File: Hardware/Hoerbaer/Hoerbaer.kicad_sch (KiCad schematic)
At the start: 41 parts, among them J1 I2C, J11 UART, J13 JTAG, J17 RST_BOOT, J2 DISPLAY, J3 uSD, J4 USB1, J5 ENCODER, SW1 RESET, SW2 PROG, U1 ESP32 S3 MINI

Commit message: Sleeping...
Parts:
- renumbered C50 to C1, C50 to C2, C50 to C3, C50 to C4, C43 to C64

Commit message: WIP new hw rev
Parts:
- removed D4: GREEN, LED_SMD:LED_0603_1608Metric, symbol Device:LED
- removed J13: JTAG, Connector_PinHeader_1.27mm:PinHeader_2x05_P1.27mm_Vertical_SMD, symbol Connector_Generic:Conn_02x05_Odd_Even
- removed R56: 5.1kΩ, Resistor_SMD:R_0402_1005Metric, symbol Device:R_Small
- removed U1: ESP32 S3 MINI, ESP32-S3-MINI-1-N8:XCVR_ESP32-S3-MINI-1-N8, symbol Baer_Symbols:ESP32-S3-MINI-1-N8
- added H4: MountingHole_Pad, MountingHole:MountingHole_3.2mm_M3_Pad_Via, symbol Mechanical:MountingHole_Pad
- added U1: ESP32-S3-WROOM-1U-N4R8, RF_Module:ESP32-S3-WROOM-1, symbol Baer_Symbols:ESP32-S3-WROOM-1
- C1, C4, C5: value 1µF, 10V -> 1µF, 16V; LCSC C29266 -> C29266
- renumbered C64 to C6, D8 to D1, D1 to D2, D2 to D3, J3 to J2, J4 to J3, J2 to J4, J11 to J5, J17 to J6, J5 to J7, R12 to R10, R14 to R11, R15 to R12, R16 to R13, R13 to R14, R10 to R15, R8 to R16, R9 to R8, R11 to R9
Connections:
- net 3V3_~{PSAVE}: now also U1.26 (IO45)
- net BAT_~{ALERT}: now also U1.16 (IO46)
- net CHG_STAT: now also U1.24 (IO47)
- net CODEC_~{PDN}: now also U1.39 (IO1)
- net DISP_CS: now also U1.5 (IO5)
- net DISP_DC: now also U1.6 (IO6)
- net DISP_RST: now also U1.7 (IO7)
- net ENC_A: now also U1.9 (IO16)
- net ENC_B: now also U1.10 (IO17)
- net ENC_BTN: now also U1.11 (IO18)
- net GND: now also H4.1, U1.1 (GND), U1.40 (GND), U1.41 (GND)
- net HBI_INT: now also U1.8 (IO15)
- net HBI_RST: now also U1.22 (IO14)
- net I2C1_SCL: now also U1.19 (IO11)
- net I2C1_SDA: now also U1.18 (IO10)
- net I2S1_BCLK: now also U1.38 (IO2)
- net I2S1_DOUT: now also U1.4 (IO4)
- net I2S1_WS: now also U1.15 (IO3)
- net MCU_IO0: now also U1.27 (IO0)
- net MCU_RXD: now also U1.36 (RXD0)
- net MCU_TXD: now also U1.37 (TXD0)
- net MCU_~{RST}: now also U1.3 (EN)
- net SD_CLK: now also U1.21 (IO13)
- net SD_CMD: now also U1.20 (IO12)
- net SD_D0: now also U1.31 (IO38)
- net SD_D1: now also U1.32 (IO39)
- net SD_D2: now also U1.33 (IO40)
- net SD_D3: now also U1.34 (IO41)
- net SD_DET: now also U1.23 (IO21)
- net SPI2_CLK: now also U1.17 (IO9)
- net SPI2_MOSI: now also U1.12 (IO8)
- net USB1_D+: now also U1.14 (USB_D+)
- net USB1_D-: now also U1.13 (USB_D-)
- net VCC: now also U1.2 (3V3); no longer C1.1, J1.4 (Pin_4), J2.4 (VDD), J4.7 (Pin_7), R1.1, R10.1, R11.1, R15.1, R16.1, R2.1, R3.1, R4.1, R7.1, R8.1, R9.1
- new net 9V_EN: U1.35 (IO42)
- new net VCC_P: C1.1, J1.4 (Pin_4), J2.4 (VDD), J4.7 (Pin_7), R1.1, R10.1, R11.1, R15.1, R16.1, R2.1, R3.1, R4.1, R7.1, R8.1, R9.1
- new net VCC_P_EN: U1.25 (IO48)
- no-connect marks 4 -> 6
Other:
- sheet Power ports: added 9V_EN, CHG_PGOOD, VCC_P_EN; removed 12V_EN
- moved on the sheet: C5, C6, J7, R14, R15, R16

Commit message: Layout, mono-jumpers
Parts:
- removed H4: MountingHole_Pad, MountingHole:MountingHole_3.2mm_M3_Pad_Via, symbol Mechanical:MountingHole_Pad
- J2: footprint Connector_Card:microSD_HC_Molex_104031-0811 -> Connector_Card:microSD_HC_Hirose_DM3D-SF; LCSC C585350 -> C719027; MPN 1040310811 -> DM3D-SF
- U1: value ESP32-S3-WROOM-1U-N4R8 -> ESP32-S3-WROOM-1-N4R8; LCSC C3013943 -> C2913200; MPN ESP32-S3-WROOM-1U-N4R8 -> ESP32-S3-WROOM-1-N4R8
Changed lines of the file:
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@@
 			)
 		)
-		(property "Footprint" "Connector_Card:microSD_HC_Molex_104031-0811"
+		(property "Footprint" "Connector_Card:microSD_HC_Hirose_DM3D-SF"
 			(at -5.08 152.4 0)
 			(effects
@@
 			)
 		)
-		(property "MPN" "1040310811"
+		(property "MPN" "DM3D-SF"
 			(at 46.99 170.18 0)
 			(effects
@@
 			)
 		)
-		(property "LCSC" "C585350"
+		(property "LCSC" "C719027"
 			(at 46.99 170.18 0)
 			(effects
@@
 	(symbol
 		(lib_id "Mechanical:MountingHole_Pad")
-		(at 209.55 158.75 0)
-		(unit 1)
-		(exclude_from_sim no)
-		(in_bom no)
-		(on_board yes)
-		(dnp no)
-		(fields_autoplaced yes)
-		(property "Reference" "H4"
-			(at 212.09 156.21 0)
-			(effects
-				(font
-					(size 1.27 1.27)
-				)
-				(justify left)
-				(hide yes)
-			)
-		)
-		(property "Value" "MountingHole_Pad"
-			(at 212.09 158.75 0)
-			(effects
-				(font
-					(size 1.27 1.27)
-				)
-				(justify left)
-				(hide yes)
-			)
-		)
-		(property "Footprint" "MountingHole:MountingHole_3.2mm_M3_Pad_Via"
-			(at 209.55 158.75 0)
-			(effects
-				(font
-					(size 1.27 1.27)
-				)
-				(hide yes)
-			)
-		)
-		(property "Datasheet" "~"
-			(at 209.55 158.75 0)
-			(effects
-				(font
-					(size 1.27 1.27)
-				)
-				(hide yes)
-			)
-		)
-		(property "Description" ""
-			(at 209.55 158.75 0)
-			(effects
-				(font
-					(size 1.27 1.27)
-				)
-			)
-		)
-		(property "Check_prices" ""
-			(at 209.55 158.75 0)
-			(effects
-				(font
-					(size 1.27 1.27)
-				)
-			)
-		)
-		(property "MANUFACTURER" ""
-			(at 209.55 158.75 0)
-			(effects
-				(font
-					(size 1.27 1.27)
-				)
-			)
-		)
-		(property "MAXIMUM_PACKAGE_HEIGHT" ""
-			(at 209.55 158.75 0)
-			(effects
-				(font
-					(size 1.27 1.27)
-				)
-			)
-		)
-		(property "MF" ""
-			(at 209.55 158.75 0)
-			(effects
-				(font
-					(size 1.27 1.27)
-				)
-			)
-		)
-		(property "MP" ""
-			(at 209.55 158.75 0)
-			(effects
-				(font
-					(size 1.27 1.27)
-				)
-			)
-		)
-		(property "PARTREV" ""
-			(at 209.55 158.75 0)
-			(effects
-				(font
-					(size 1.27 1.27)
-				)
-			)
-		)
-		(property "Package" ""
-			(at 209.55 158.75 0)
-			(effects
-				(font
-					(size 1.27 1.27)
-				)
-			)
-		)
-		(property "Price" ""
-			(at 209.55 158.75 0)
-			(effects
-				(font
-					(size 1.27 1.27)
-				)
-			)
-		)
-		(property "Purchase-URL" ""
-			(at 209.55 158.75 0)
-			(effects
-				(font
-					(size 1.27 1.27)
-				)
-			)
-		)
-		(property "STANDARD" ""
-			(at 209.55 158.75 0)
-			(effects
-				(font
-					(size 1.27 1.27)
-				)
-			)
-		)
-		(property "SnapEDA_Link" ""
-			(at 209.55 158.75 0)
-			(effects
-				(font
-					(size 1.27 1.27)
-				)
-			)
-		)
-		(pin "1"
-		)
-		(instances
-			(project "Hoerbaer"
-				(path "/31f16f54-0469-45ae-b442-d363bf5fad3b"
-					(reference "H4")
-					(unit 1)
-				)
-			)
-		)
-	)
-	(symbol
-		(lib_id "Mechanical:MountingHole_Pad")
 		(at 194.31 158.75 0)
 		(unit 1)
@@
 			)
 		)
-		(property "Value" "ESP32-S3-WROOM-1U-N4R8"
+		(property "Value" "ESP32-S3-WROOM-1-N4R8"
 			(at 142.748 73.66 0)
 			(effects
@@
 			)
 		)
-		(property "LCSC" "C3013943"
+		(property "LCSC" "C2913200"
 			(at 154.94 106.68 0)
 			(effects
@@
 			)
 		)
-		(property "MPN" "ESP32-S3-WROOM-1U-N4R8 "
+		(property "MPN" "ESP32-S3-WROOM-1-N4R8"
 			(at 154.94 106.68 0)
 			(effects
@@
 					(unit 1)
 				)
-			)
-		)
-	)
-	(symbol
-		(lib_id "power:GND")
-		(at 209.55 161.29 0)
-		(mirror y)
-		(unit 1)
-		(exclude_from_sim no)
-		(in_bom yes)
-		(on_board yes)
-		(dnp no)
-		(property "Reference" "#PWR0199"
-			(at 209.55 167.64 0)
-			(effects
-				(font
-					(size 1.27 1.27)
-				)
-				(hide yes)
-			)
-		)
-		(property "Value" "GND"
-			(at 213.36 163.83 0)
-			(effects
-				(font
-					(size 1.27 1.27)
-				)
-			)
-		)
-		(property "Footprint" ""
-			(at 209.55 161.29 0)
-			(effects
-				(font
-					(size 1.27 1.27)
-				)
-				(hide yes)
-			)
-		)
-		(property "Datasheet" ""
-			(at 209.55 161.29 0)
-			(effects
-				(font
-					(size 1.27 1.27)
-				)
-				(hide yes)
-			)
-		)
-		(property "Description" ""
-			(at 209.55 161.29 0)
-			(effects
-				(font
-					(size 1.27 1.27)
-				)
-			)
-		)
-		(pin "1"
-		)
-		(instances
-			(project "Hoerbaer"
-				(path "/31f16f54-0469-45ae-b442-d363bf5fad3b"
-					(reference "#PWR0199")
-					(unit 1)
-				)

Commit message: Layout rev 2 - without silkscreen
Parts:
- J1: footprint Connector_PinHeader_2.54mm:PinHeader_1x04_P2.54mm_Vertical -> Connector_PinHeader_2.54mm:PinHeader_2x02_P2.54mm_Vertical
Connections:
- net BAT_~{ALERT}: now also U1.39 (IO1); no longer U1.16 (IO46)
- net CODEC_~{PDN}: now also U1.22 (IO14); no longer U1.39 (IO1)
- net DISP_CS: now also U1.11 (IO18); no longer U1.5 (IO5)
- net DISP_DC: now also U1.12 (IO8); no longer U1.6 (IO6)
- net DISP_RST: now also U1.38 (IO2); no longer U1.7 (IO7)
- net ENC_A: now also U1.4 (IO4); no longer U1.9 (IO16)
- net ENC_B: now also U1.5 (IO5); no longer U1.10 (IO17)
- net ENC_BTN: now also U1.6 (IO6); no longer U1.11 (IO18)
- net HBI_INT: now also U1.7 (IO7); no longer U1.8 (IO15)
- net HBI_RST: now also U1.8 (IO15); no longer U1.22 (IO14)
- net I2C1_SCL: now also J1.3 (Pin_3); no longer J1.2 (Pin_2)
- net I2C1_SDA: now also J1.4 (Pin_4); no longer J1.3 (Pin_3)
- net I2S1_BCLK: now also U1.16 (IO46); no longer U1.38 (IO2)
- net I2S1_DOUT: now also U1.17 (IO9); no longer U1.4 (IO4)
- net SPI2_CLK: now also U1.10 (IO17); no longer U1.17 (IO9)
- net SPI2_MOSI: now also U1.9 (IO16); no longer U1.12 (IO8)
- net VCC_P: now also J1.2 (Pin_2); no longer J1.4 (Pin_4)
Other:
- moved on the sheet: R1, R2

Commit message: BOM FIxes
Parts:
- C6: LCSC C458949 -> C1525; MPN MT15B104K160CT -> CL05B104KO5NNNC
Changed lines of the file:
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@@
 			)
 		)
-		(property "LCSC" "C458949"
+		(property "LCSC" "C1525"
 			(at 248.92 157.48 0)
 			(effects
@@
 			)
 		)
-		(property "MPN" "MT15B104K160CT"
+		(property "MPN" "CL05B104KO5NNNC"
 			(at 248.92 157.48 0)
 			(effects

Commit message: Production
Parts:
- J1, J4, J5, J6, J7: FT Rotation Offset (none) -> 90; JLCPCB Rotation Offset 90 -> (none)
- J3: FT Position Offset (none) -> 0.0,1.35; JLCPCB Position Offset 0.0,1.35 -> (none)
- U1: FT Position Offset (none) -> 0.0,-3.63
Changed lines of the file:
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@@
 			)
 		)
-		(property "JLCPCB Rotation Offset" "90"
-			(at 82.55 33.02 0)
-			(effects
-				(font
-					(size 1.27 1.27)
-				)
-				(hide yes)
-			)
-		)
 		(property "Check_prices" ""
 			(at 82.55 33.02 0)
@@
 			)
 		)
+		(property "FT Rotation Offset" "90"
+			(at 82.55 33.02 0)
+			(effects
+				(font
+					(size 1.27 1.27)
+				)
+			)
+		)
 		(pin "1"
 		)
@@
 			)
 		)
-		(property "JLCPCB Rotation Offset" "90"
-			(at 273.05 154.94 0)
-			(effects
-				(font
-					(size 1.27 1.27)
-				)
-				(hide yes)
-			)
-		)
 		(property "Check_prices" ""
 			(at 273.05 154.94 0)
@@
 			)
 		)
+		(property "FT Rotation Offset" "90"
+			(at 273.05 154.94 0)
+			(effects
+				(font
+					(size 1.27 1.27)
+				)
+			)
+		)
 		(pin "1"
 		)
@@
 			)
 		)
-		(property "JLCPCB Rotation Offset" "90"
-			(at 203.2 30.48 0)
-			(effects
-				(font
-					(size 1.27 1.27)
-				)
-				(hide yes)
-			)
-		)
 		(property "Check_prices" ""
 			(at 203.2 30.48 0)
@@
 			)
 		)
+		(property "FT Rotation Offset" "90"
+			(at 203.2 30.48 0)
+			(effects
+				(font
+					(size 1.27 1.27)
+				)
+			)
+		)
 		(pin "1"
 		)
@@
 			)
 		)
-		(property "JLCPCB Rotation Offset" "90"
-			(at 205.74 52.07 0)
-			(effects
-				(font
-					(size 1.27 1.27)
-				)
-				(hide yes)
-			)
-		)
 		(property "Check_prices" ""
 			(at 205.74 52.07 0)
@@
 			)
 		)
+		(property "FT Rotation Offset" "90"
+			(at 205.74 52.07 0)
+			(effects
+				(font
+					(size 1.27 1.27)
+				)
+			)
+		)
 		(pin "1"
 		)
@@
 			)
 		)
-		(property "JLCPCB Rotation Offset" "90"
-			(at 30.48 33.02 0)
-			(effects
-				(font
-					(size 1.27 1.27)
-				)
-				(hide yes)
-			)
-		)
 		(property "Check_prices" ""
 			(at 30.48 33.02 0)
@@
 			)
 		)
+		(property "FT Rotation Offset" "90"
+			(at 30.48 33.02 0)
+			(effects
+				(font
+					(size 1.27 1.27)
+				)
+			)
+		)
 		(pin "1"
 		)
@@
 			)
 		)
+		(property "FT Position Offset" "0.0,-3.63"
+			(at 154.94 106.68 0)
+			(effects
+				(font
+					(size 1.27 1.27)
+				)
+				(hide yes)
+			)
+		)
 		(pin "22"
 		)
@@
 			)
 		)
-		(property "JLCPCB Position Offset" "0.0,1.35"
-			(at 66.04 88.9 0)
-			(effects
-				(font
-					(size 1.27 1.27)
-				)
-				(hide yes)
-			)
-		)
 		(property "Check_prices" ""
 			(at 66.04 88.9 0)
@@
 			(at 66.04 88.9 0)
 			(effects
+				(font
+					(size 1.27 1.27)
+				)
+			)
+		)
+		(property "FT Position Offset" "0.0,1.35"
+			(at 66.04 88.9 0)
+			(effects

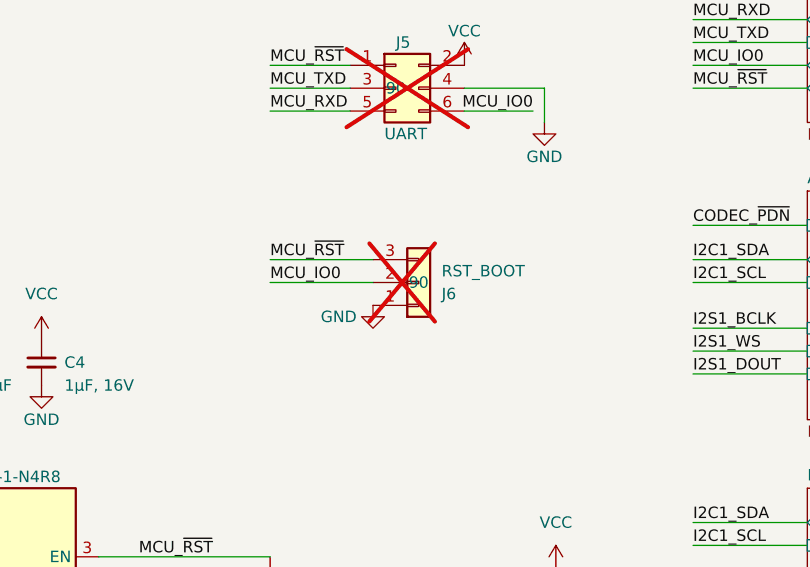
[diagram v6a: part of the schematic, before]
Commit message: Layout fixes (production feedback)
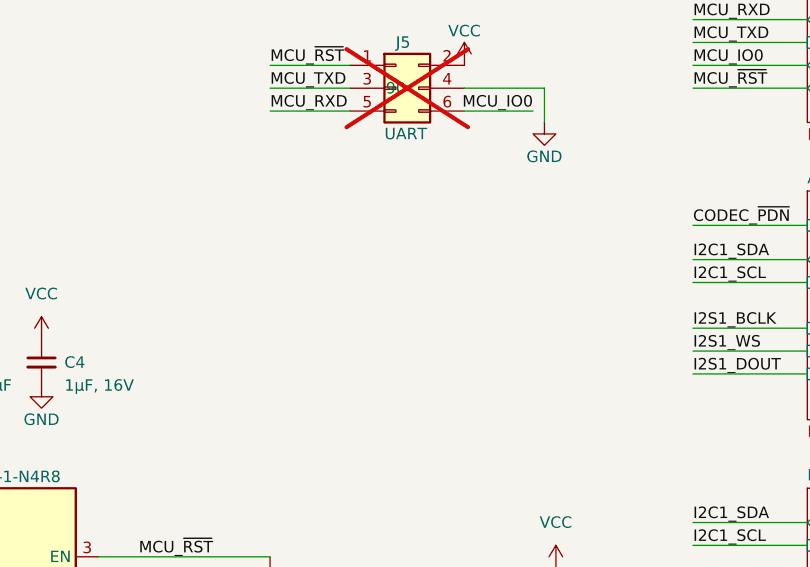
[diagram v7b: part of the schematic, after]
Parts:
- removed J6: RST_BOOT, Connector_PinHeader_2.54mm:PinHeader_1x03_P2.54mm_Vertical, symbol Connector_Generic:Conn_01x03
